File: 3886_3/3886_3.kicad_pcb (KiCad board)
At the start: 2 copper layers, 95 x 78 mm, 59 parts, among them J101 2, J102 2, J103 3, Q101 BT139-600E, Q102 BC817, Q103 BC807, U101 LM3886TF

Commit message: Add files via upload
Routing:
- net Net-(D105--): track 25.2 -> 29.4 mm
- net GND: vias 13 -> 12
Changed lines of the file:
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@@
-	)
-	(via
-		(at 57.15 66.802)
-		(size 3)
-		(drill 1.2)
-		(layers "F.Cu" "B.Cu")
-		(free yes)
-		(tenting none)
-		(net 2)
 	)
 	(via
@@
 	)
 	(segment
-		(start 41.269 108.198)
-		(end 46.99 113.919)
-		(width 4.5)
+		(start 61.849 113.538)
+		(end 48.26 113.538)
+		(width 4)
 		(layer "B.Cu")
 		(net 19)
 	)
 	(segment
-		(start 60.452 114.046)
-		(end 47.752 114.046)
-		(width 5)
+		(start 47.371 113.538)
+		(end 50.419 113.538)
+		(width 4)
 		(layer "B.Cu")
 		(net 19)
 	)
 	(segment
+		(start 42.031 108.198)
+		(end 47.371 113.538)
+		(width 4)
+		(layer "B.Cu")
+		(net 19)
+	)
+	(segment
 		(start 36.83 108.198)
-		(end 41.269 108.198)
+		(end 42.031 108.198)
 		(width 4)
 		(layer "B.Cu")
@@
 	)
 	(segment
-		(start 49.022 108.198)
-		(end 49.022 106.68)
-		(width 4.5)
+		(start 57.658 98.298)
+		(end 49.022 106.934)
+		(width 4)
 		(layer "B.Cu")
 		(net 22)
 	)
 	(segment
-		(start 57.658 98.298)
-		(end 49.276 106.68)
-		(width 5)
+		(start 49.022 106.934)
+		(end 49.022 108.198)
+		(width 4)
 		(layer "B.Cu")
 		(net 22)
 	)
 	(segment
-		(start 57.658 98.298)
-		(end 61.849 98.298)
+		(start 61.849 98.298)
+		(end 57.658 98.298)
 		(width 4)
 		(layer "B.Cu")
@@
 			(pts
 				(xy 45.974 110.236) (xy 36.83 110.236) (xy 36.83 105.2576) (xy 46.1264 105.2576) (xy 50.8 100.584)
-				(xy 50.8 80.01) (xy 51.816 80.01) (xy 51.816 94.996) (xy 59.436 94.996) (xy 59.436 99.06) (xy 77.724 99.06)
+				(xy 50.8 80.01) (xy 51.816 80.01) (xy 51.816 95.758) (xy 59.436 95.758) (xy 59.436 99.06) (xy 77.724 99.06)
 				(xy 77.724 93.853) (xy 82.55 93.853) (xy 82.55 101.981) (xy 77.216 101.981) (xy 77.216 114.554)
-				(xy 65.278 114.554) (xy 65.278 117.221) (xy 45.974 117.221)
+				(xy 65.278 114.554) (xy 65.278 116.332) (xy 45.974 116.332)
 			)
 		)
@@
 		(polygon
 			(pts
-				(xy 45.974 117.475) (xy 77.216 117.475) (xy 77.216 112.522) (xy 80.01 112.522) (xy 80.01 119.38)
-				(xy 45.212 119.38) (xy 37.719 111.633) (xy 30.607 111.633) (xy 30.607 110.744) (xy 35.56 110.744)
+				(xy 45.974 117.475) (xy 77.724 117.475) (xy 77.724 112.522) (xy 79.502 112.522) (xy 79.502 119.126)
+				(xy 44.958 119.126) (xy 37.719 111.633) (xy 30.607 111.633) (xy 30.607 110.744) (xy 35.56 110.744)
 				(xy 39.37 110.744)
 			)
@@
 		(polygon
 			(pts
-				(xy 57.658 65.024) (xy 57.658 68.58) (xy 54.102 68.58) (xy 54.102 65.024)
+				(xy 57.658 65.024) (xy 58.928 66.294) (xy 58.928 68.58) (xy 54.102 68.58) (xy 54.102 65.024)
 			)
 		)

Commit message: Add files via upload
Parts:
- moved R121 0.25 mm to (51.3, 91.7)
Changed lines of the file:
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@@
 	(footprint "Resistor_SMD:R_2512_6332Metric_Pad1.40x3.35mm_HandSolder"
 		(layer "B.Cu")
-		(at 51.31 91.44 180)
+		(at 51.31 91.694 180)
 		(descr "Resistor SMD 2512 (6332 Metric), square (rectangular) end terminal, IPC-7351 nominal with elongated pad for handsoldering. (Body size source: IPC-SM-782 page 72, https://www.pcb-3d.com/wordpress/wp-content/uploads/ipc-sm-782a_amendment_1_and_2.pdf), generated with kicad-footprint-generator")
 		(tags "resistor handsolder")

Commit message: Add files via upload
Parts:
- removed C120, C121: 100n, Capacitor_SMD:C_1206_3216Metric_Pad1.33x1.80mm_HandSolder
- moved C122 0.51 mm to (61.5, 53.3)
- moved C123 0.51 mm to (61.5, 47.1)
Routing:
- net VN: track 116.8 -> 114.7 mm
- net VP: track 80.0 -> 78.0 mm
- net Net-(R105-Pad1): track 34.5 -> 33.6 mm

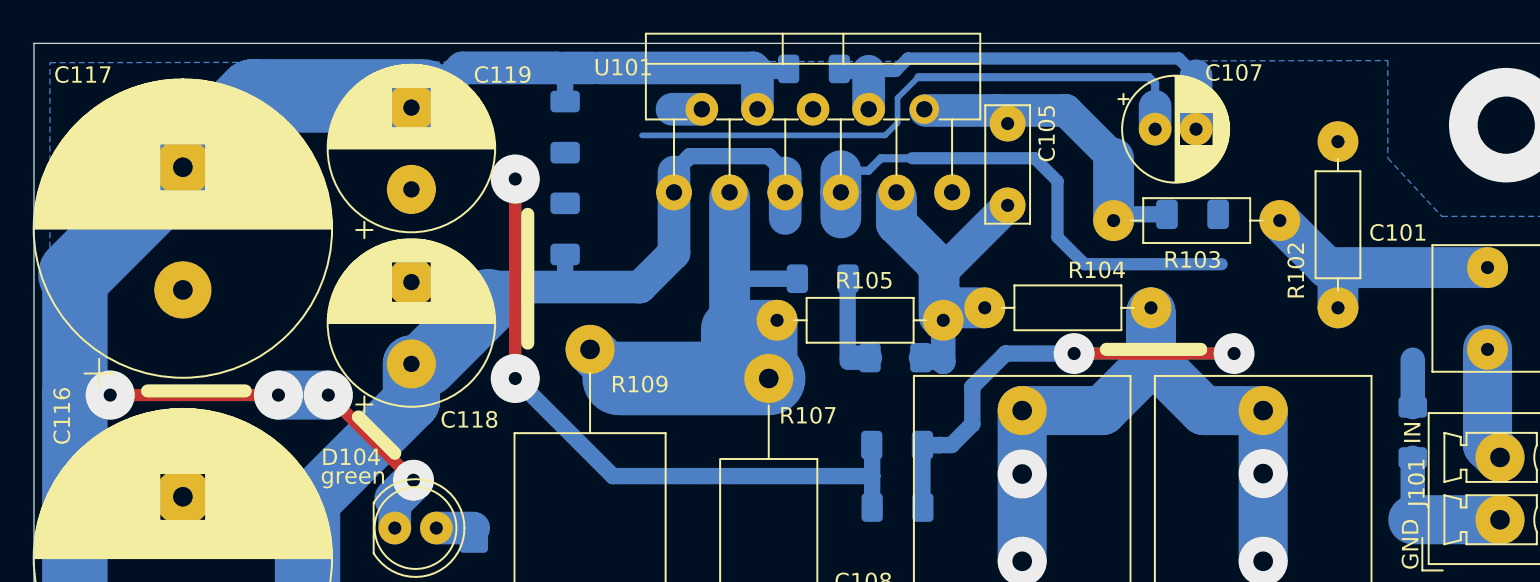
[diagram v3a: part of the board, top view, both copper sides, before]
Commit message: Add files via upload
supply caps removed
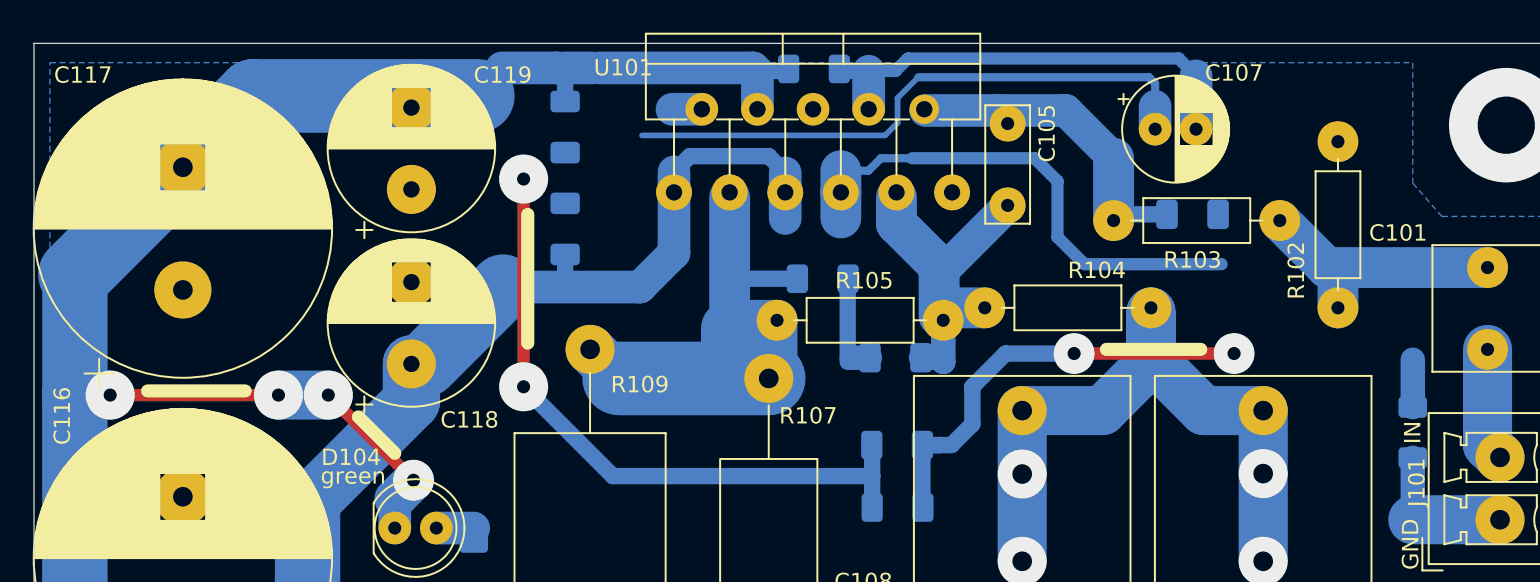
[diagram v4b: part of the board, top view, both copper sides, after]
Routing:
- net VP: track 78.0 -> 79.2 mm
- net VN: track 114.7 -> 115.9 mm
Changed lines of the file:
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@@
-	)
-	(segment
-		(start 58.42 62.484)
-		(end 58.42 50.292)
-		(width 0.75)
-		(layer "F.Cu")
-		(net 2)
 	)
 	(segment
@@
 		(end 91.694 103.886)
 		(width 1)
+		(layer "F.Cu")
+		(net 2)
+	)
+	(segment
+		(start 58.928 62.992)
+		(end 58.928 50.292)
+		(width 0.75)
 		(layer "F.Cu")
 		(net 2)
@@
 	)
 	(via
-		(at 58.42 62.484)
+		(at 58.928 62.992)
 		(size 3)
 		(drill 0.8)
@@
 	)
 	(via
-		(at 58.42 50.292)
+		(at 58.928 50.292)
 		(size 3)
 		(drill 0.8)
@@
 	)
 	(segment
+		(start 58.928 62.992)
+		(end 64.389 68.453)
+		(width 1)
+		(layer "B.Cu")
+		(net 2)
+	)
+	(segment
 		(start 83.321 66.548)
 		(end 83.312 66.557)
 		(width 0.75)
-		(layer "B.Cu")
-		(net 2)
-	)
-	(segment
-		(start 64.389 68.453)
-		(end 80.238 68.453)
-		(width 1)
 		(layer "B.Cu")
 		(net 2)
@@
 	)
 	(segment
-		(start 58.42 62.484)
-		(end 64.389 68.453)
-		(width 1)
-		(layer "B.Cu")
-		(net 2)
-	)
-	(segment
 		(start 80.238 68.453)
 		(end 80.238 66.583)
@@
 		(end 97.536 45.847)
 		(width 2)
+		(layer "B.Cu")
+		(net 2)
+	)
+	(segment
+		(start 64.389 68.453)
+		(end 80.238 68.453)
+		(width 1)
 		(layer "B.Cu")
 		(net 2)
@@
 	)
 	(segment
+		(start 52.959 61.595)
+		(end 57.658 56.896)
+		(width 4)
+		(layer "B.Cu")
+		(net 6)
+	)
+	(segment
 		(start 68.961 49.022)
 		(end 69.088 48.895)
@@
 		(end 61.468 54.9025)
 		(width 1)
-		(layer "B.Cu")
-		(net 6)
-	)
-	(segment
-		(start 52.959 61.595)
-		(end 56.769 57.785)
-		(width 4)
 		(layer "B.Cu")
 		(net 6)
@@
 	)
 	(segment
+		(start 57.592 43.5)
+		(end 60.959 43.5)
+		(width 2)
+		(layer "B.Cu")
+		(net 7)
+	)
+	(segment
 		(start 72.965 43.501)
 		(end 63.5 43.501)
@@
 	)
 	(segment
-		(start 55.179 43.5)
-		(end 60.959 43.5)
+		(start 56.134 45.212)
+		(end 53.467 45.212)
 		(width 2)
 		(layer "B.Cu")
@@
 		(end 75.132 43.561)
 		(width 1)
+		(layer "B.Cu")
+		(net 7)
+	)
+	(segment
+		(start 53.467 45.212)
+		(end 52.752 45.927)
+		(width 2)
 		(layer "B.Cu")
 		(net 7)
@@
 	)
 	(segment
-		(start 52.07 45.927)
-		(end 52.752 45.927)
-		(width 2)
-		(layer "B.Cu")
-		(net 7)
-	)
-	(segment
 		(start 51.054 71.628)
 		(end 51.054 69.85)
@@
 	)
 	(segment
-		(start 52.752 45.927)
-		(end 55.179 43.5)
-		(width 2)
-		(layer "B.Cu")
-		(net 7)
-	)
-	(segment
-		(start 52.785 45.212)
-		(end 42.418 45.212)
-		(width 4.5)
-		(layer "B.Cu")
-		(net 7)
-	)
-	(segment
 		(start 61.468 43.501)
 		(end 61.468 45.5545)
 		(width 1)
+		(layer "B.Cu")
+		(net 7)
+	)
+	(segment
+		(start 63.373 43.628)
+		(end 63.5 43.501)
+		(width 0.75)
+		(layer "B.Cu")
+		(net 7)
+	)
+	(segment
+		(start 64.516 43.501)
+		(end 63.5 43.501)
+		(width 1)
+		(layer "B.Cu")
+		(net 7)
+	)
+	(segment
+		(start 31.5 56.13)
+		(end 31.5 63.5)
+		(width 4)
+		(layer "B.Cu")
+		(net 7)
+	)
+	(segment
+		(start 52.752 45.927)
+		(end 52.07 45.927)
+		(width 2)
+		(layer "B.Cu")
+		(net 7)
+	)
+	(segment
+		(start 31.496 63.5)
+		(end 31.496 83.439)
+		(width 4)
 		(layer "B.Cu")
 		(net 7)
@@
 	)
 	(segment
-		(start 63.373 43.628)
-		(end 63.5 43.501)
-		(width 0.75)
-		(layer "B.Cu")
-		(net 7)
-	)
-	(segment
-		(start 64.516 43.501)
-		(end 63.5 43.501)
-		(width 1)
-		(layer "B.Cu")
-		(net 7)
-	)
-	(segment
-		(start 31.5 56.13)
-		(end 31.5 63.5)
-		(width 4)
-		(layer "B.Cu")
-		(net 7)
-	)
-	(segment
-		(start 31.496 63.5)
-		(end 31.496 83.439)
-		(width 4)
-		(layer "B.Cu")
-		(net 7)
-	)
-	(segment
 		(start 60.959 43.5)
 		(end 60.96 43.501)
 		(width 2)
+		(layer "B.Cu")
+		(net 7)
+	)
+	(segment
+		(start 56.134 45.212)
+		(end 42.418 45.212)
+		(width 4.5)
 		(layer "B.Cu")
 		(net 7)
@@
 		(polygon
 			(pts
-				(xy 29.972 43.18) (xy 111.76 43.053) (xy 111.76 49.022) (xy 115.062 52.578) (xy 123.19 52.578) (xy 123.19 119.634)
-				(xy 29.972 119.634)
+				(xy 29.972 43.18) (xy 113.284 43.18) (xy 113.284 50.546) (xy 115.062 52.578) (xy 123.19 52.578)
+				(xy 123.19 119.634) (xy 29.972 119.634)
 			)
 		)
@@
 				(xy 108.966 62.738) (xy 108.966 91.44) (xy 106.426 93.98) (xy 90.678 93.98) (xy 87.884 91.186) (xy 87.884 62.992)
 				(xy 100.838 62.992) (xy 100.838 50.038) (xy 103.124 50.038) (xy 103.124 41.783) (xy 66.421 41.783)
-				(xy 66.421 55.372) (xy 59.182 55.372) (xy 59.182 59.944) (xy 52.578 59.944) (xy 52.578 65.532) (xy 57.658 65.532)
-				(xy 60.452 68.326) (xy 60.452 70.866) (xy 62.992 73.406) (xy 65.278 73.406) (xy 79.756 73.406) (xy 82.55 75.946)
+				(xy 66.421 55.372) (xy 59.182 55.372) (xy 59.182 59.944) (xy 52.578 59.944) (xy 52.578 65.532) (xy 57.15 65.532)
+				(xy 58.674 67.056) (xy 58.674 68.58) (xy 63.5 73.406) (xy 65.278 73.406) (xy 79.756 73.406) (xy 82.55 75.946)
 				(xy 82.55 90.678) (xy 82.55 120.65) (xy 124.46 120.65) (xy 124.46 62.738)
 			)
@@
 		(polygon
 			(pts
-				(xy 57.658 65.532) (xy 58.928 66.802) (xy 58.928 68.58) (xy 54.102 68.58) (xy 54.102 65.532)
+				(xy 57.15 65.532) (xy 58.42 66.802) (xy 58.42 68.58) (xy 54.102 68.58) (xy 54.102 65.532)
 			)
 		)
